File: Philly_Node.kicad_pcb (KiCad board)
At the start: 2 copper layers, 22 x 39 mm, 72 parts, among them J1 *, J2 LED, J4 USB_C_Receptacle_USB2.0, J5 Multi, Q1 Q_Dual_NMOS_G1S2G2D2S1D1, Q4 Q_NMOS_GSD, SW2 D0, U1 BQ25176JDSGR, U2 MDBT50Q-U1MV2, U3 E22-900M22S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

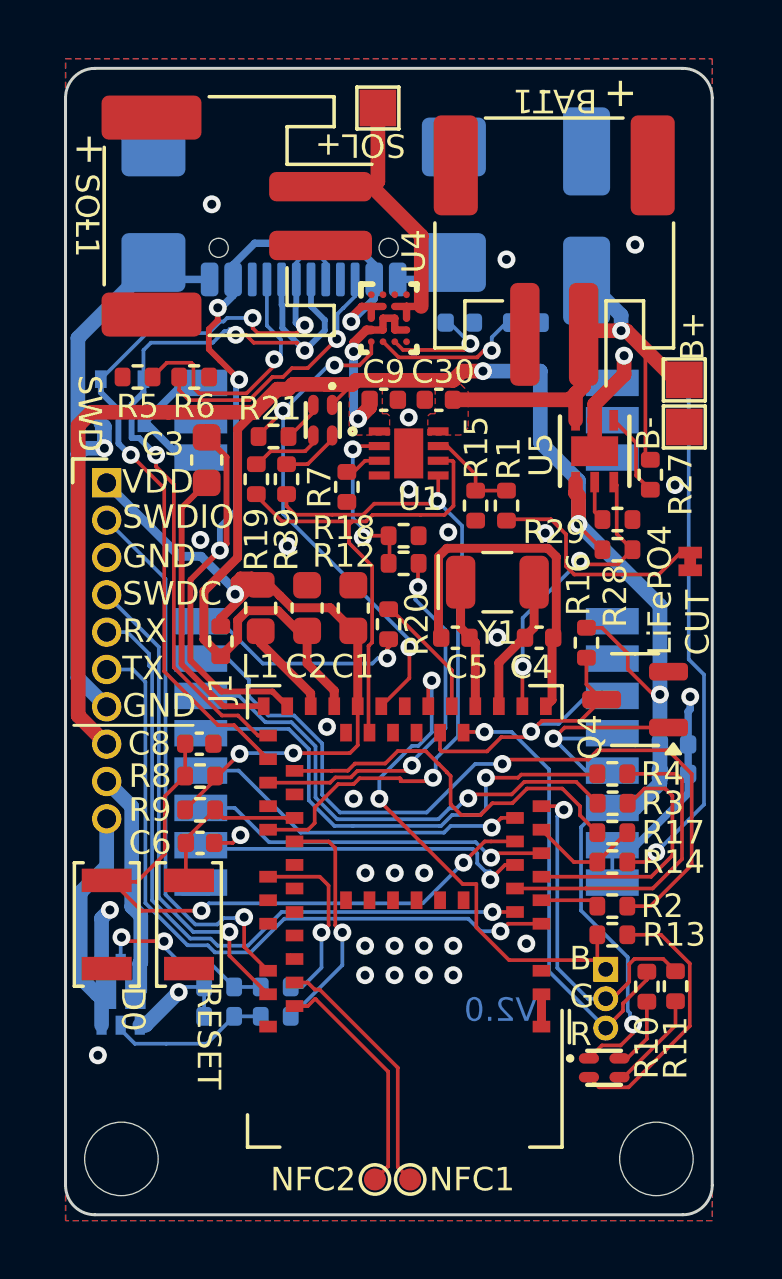
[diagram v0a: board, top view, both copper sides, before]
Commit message: Add 2 user inputs with ESD diodes, break out old analog battery voltage monitor pin.
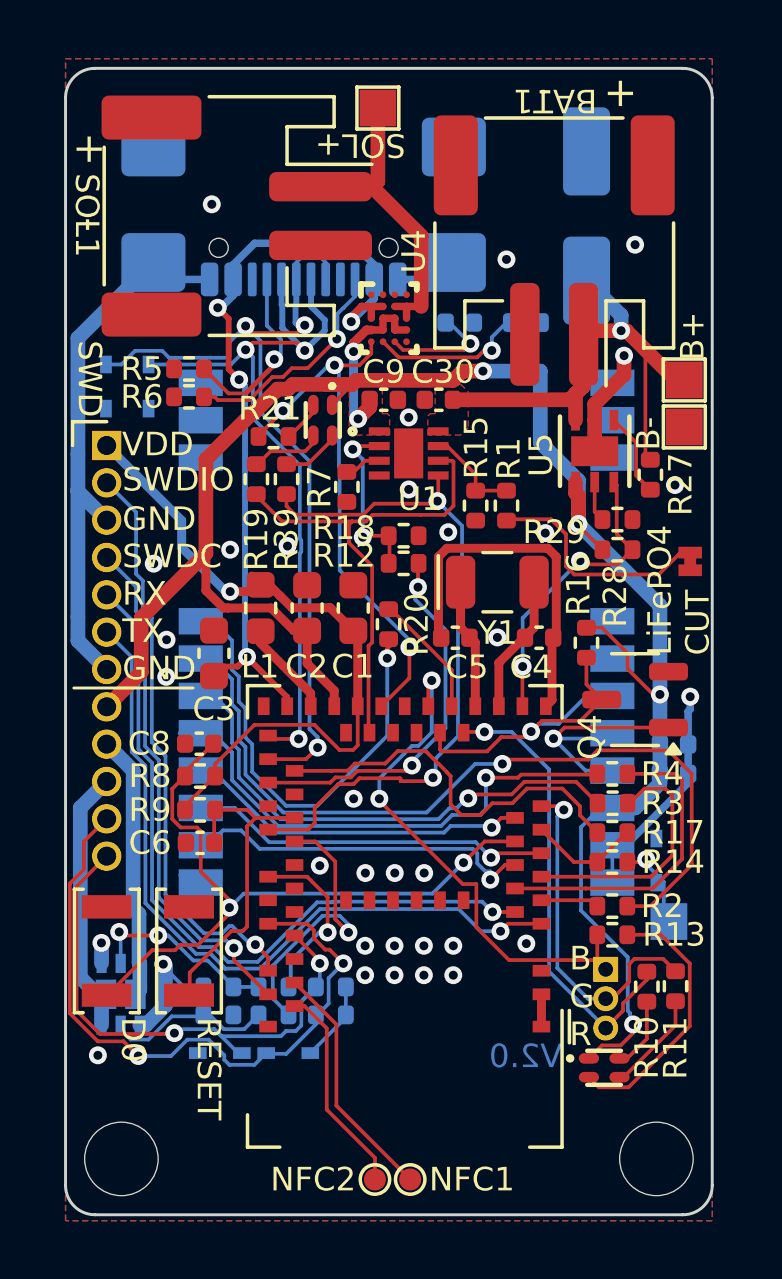
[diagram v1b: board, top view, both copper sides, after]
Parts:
- removed J1: *, Philly_Lib:R_0402_1005Metric
- added D3: LESD5D5_0CT1G, Philly_Lib:SOD-523_L1.2-W0.8-LS1.6-BI, B.Cu at (87.6, 78.5)
- added D4: LESD5D5_0CT1G, Philly_Lib:SOD-523_L1.2-W0.8-LS1.6-BI, B.Cu at (85.2, 78.5)
- added D5: LESD5D5_0CT1G, Philly_Lib:SOD-523_L1.2-W0.8-LS1.6-BI, B.Cu at (100.1, 72.0)
- added R30: 300k, Philly_Lib:R_0402_1005Metric, B.Cu at (89.0, 77.2)
- added R31: 300k, Philly_Lib:R_0402_1005Metric, B.Cu at (89.0, 76.2)
- added TP4: TestPoint, Philly_Lib:TestPoint_Pad_1.0x1.0mm, B.Cu at (100.5, 74.0)
- J5: footprint Philly_Lib:PinHeader_1x10_P1.27mm_Vertical -> Philly_Lib:PinHeader_1x12_P1.27mm_Vertical
- moved C3 6.58 mm to (85.0, 64.9), turned to -90 degrees
- moved R5 1.77 mm to (84.2, 55.2)
- moved J5 1.27 mm to (81.4, 57.8)
- moved RESET1 0.90 mm to (84.2, 75.0), turned to 90 degrees
- moved SW2 0.90 mm to (81.4, 75.0), turned to 90 degrees
- moved R6 0.70 mm to (84.2, 56.2), turned to 0 degrees
- moved D1 0.53 mm to (82.8, 55.8)
- moved D2 0.53 mm to (81.4, 55.8)
- moved R22 0.09 mm to (87.1, 77.2)
- moved R24 0.08 mm to (87.1, 76.2)
- moved R23 0.06 mm to (85.2, 77.2), turned to 0 degrees
- turned C6 to 180 degrees
- turned C8 to 180 degrees
- renumbered D4 to D1, D5 to D2
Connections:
- R14 pad 1: /VBAT_UNFUSED -> AIN7
- U2 pad 48: unconnected-(U2-P0.24-Pad48) -> P0.24
- U2 pad 49: unconnected-(U2-P0.25-Pad49) -> P0.25
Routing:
- net P0.24: track 0.00 -> 23.5 mm, vias 0 -> 2
- net /VBAT_UNFUSED: track 41.8 -> 21.0 mm, vias 2 -> 1
- net P0.25: track 0.00 -> 19.7 mm, vias 0 -> 2
- net /VBAT_POL_PROT: track 80.8 -> 67.0 mm
- net GND: track 72.1 -> 59.0 mm, vias 32 -> 33
- net Net-(U3-NSS): track 7.63 -> 16.1 mm
- net Net-(U2-~{RESET}/P0.18): track 5.71 -> 11.3 mm
- net /VBUS: track 32.8 -> 27.3 mm
- net AIN7: track 0.00 -> 3.34 mm, vias 0 -> 1
- net D0: track 21.4 -> 23.7 mm
- net P0.19: track 8.04 -> 9.92 mm
- net P1.12_RX: track 23.6 -> 25.2 mm
- net P1.11_TX: track 23.9 -> 25.4 mm
- net NMOS_2: track 7.99 -> 9.42 mm
- net Net-(J4-CC2): track 9.15 -> 7.76 mm
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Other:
- board text added: "24"
- board text added: "25"
- board text added: "AIN7"
- board text added: "N1"
- board text added: "N2"
- board text removed: "O19­↓"
- board text removed: "O20→"

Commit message: Beginning of board adjustments to use multiple fabs.
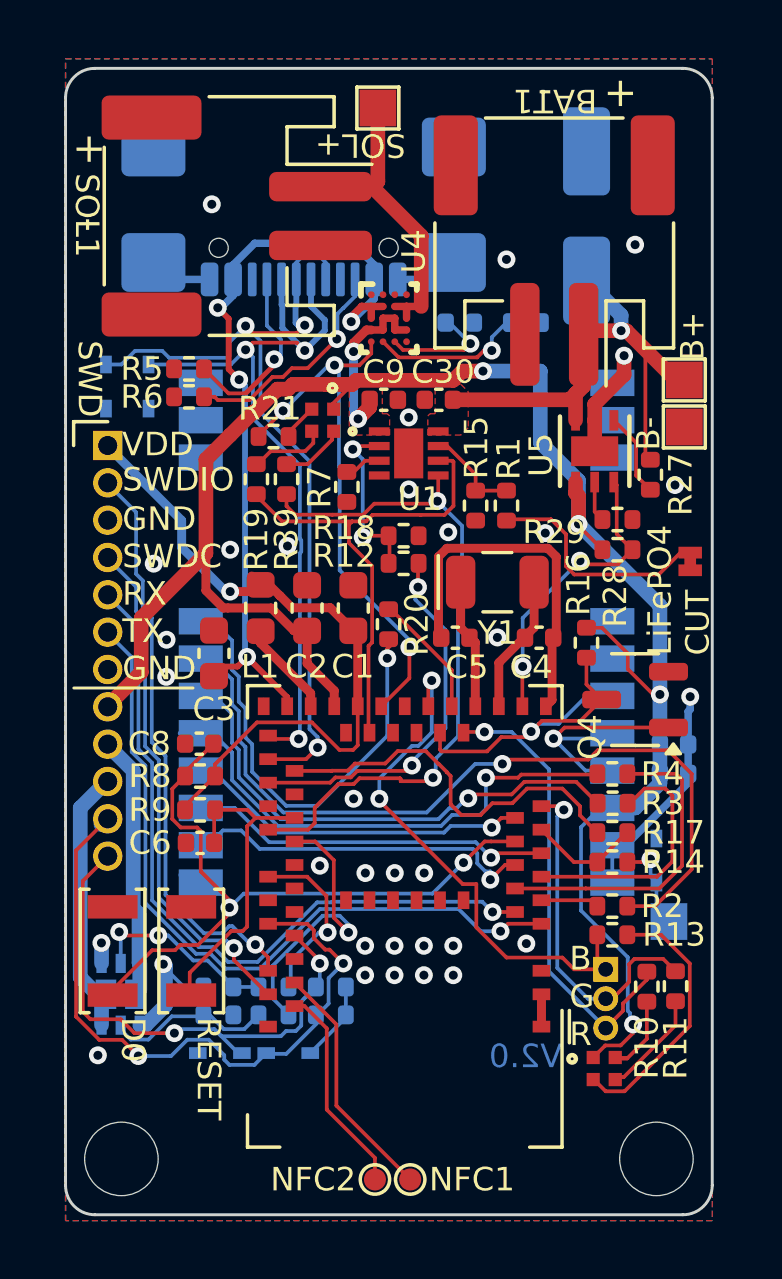
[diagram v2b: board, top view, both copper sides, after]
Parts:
- LED1, LED2: value MHPA1010RGBDT -> L201DS-QEPGBG2S; footprint Philly_Lib:LED-ARRAY-SMD_4P-L1.0-W1.0-TR-RD -> Philly_Lib:L201DS-QEPGBG2S
- moved SW2 0.20 mm to (81.6, 75.0)
- moved RESET1 0.08 mm to (84.3, 75.0)
- turned LED1 to 0 degrees
- turned LED2 to -90 degrees
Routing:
- net GND: track 59.0 -> 40.8 mm
